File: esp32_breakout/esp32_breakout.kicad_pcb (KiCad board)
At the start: 2 copper layers, 73.1 x 33.1 mm, 29 parts, among them J1 JST B7B-PH-K-S, J2 JST B7B-PH-K-S, J3 JST B6B-PH-K-S, J4 XT30U-M, J5 JST B5B-PH-K-S, J6 DNP, J7 DNP, J8 JST B6B-ZR, J9 JST B6B-ZR, SW1 SS12D10, U1 ESP32 DEV KIT Module 30-pin, U2 LM2596 Module

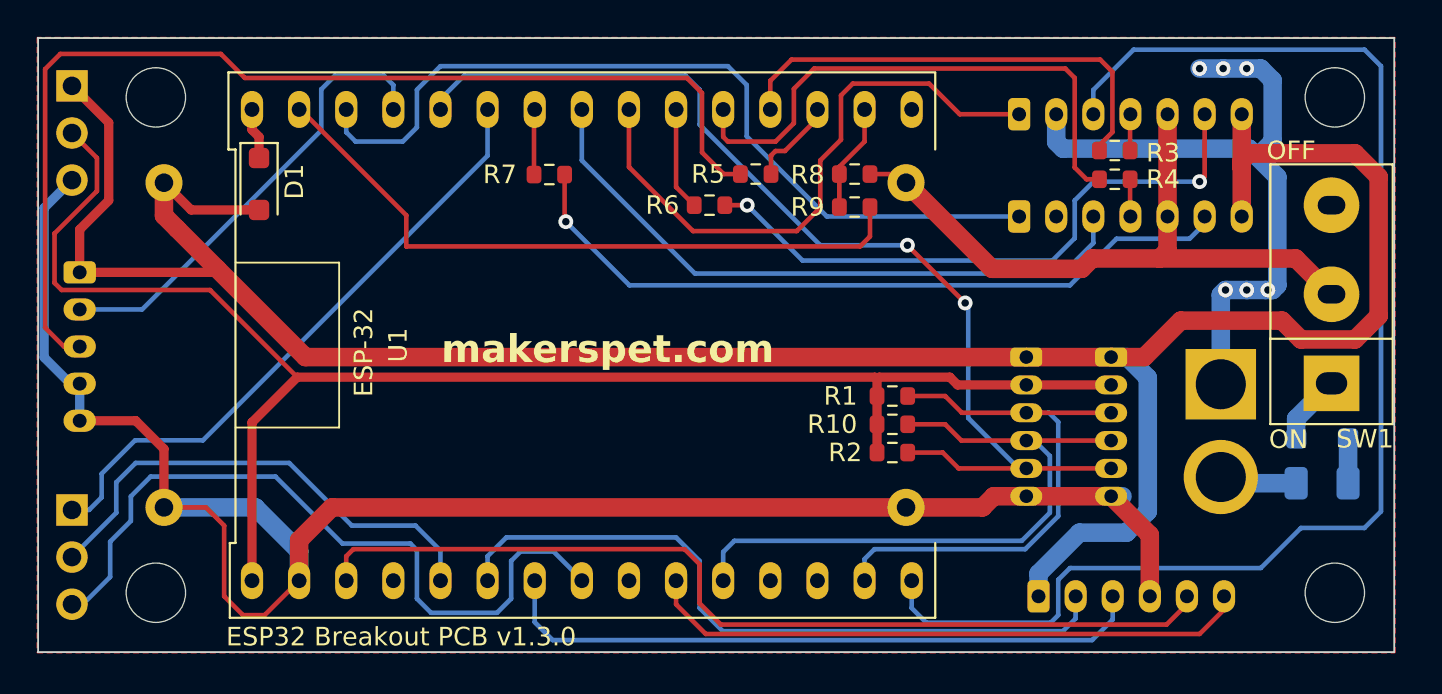
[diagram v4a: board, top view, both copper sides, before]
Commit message: ZH connectors
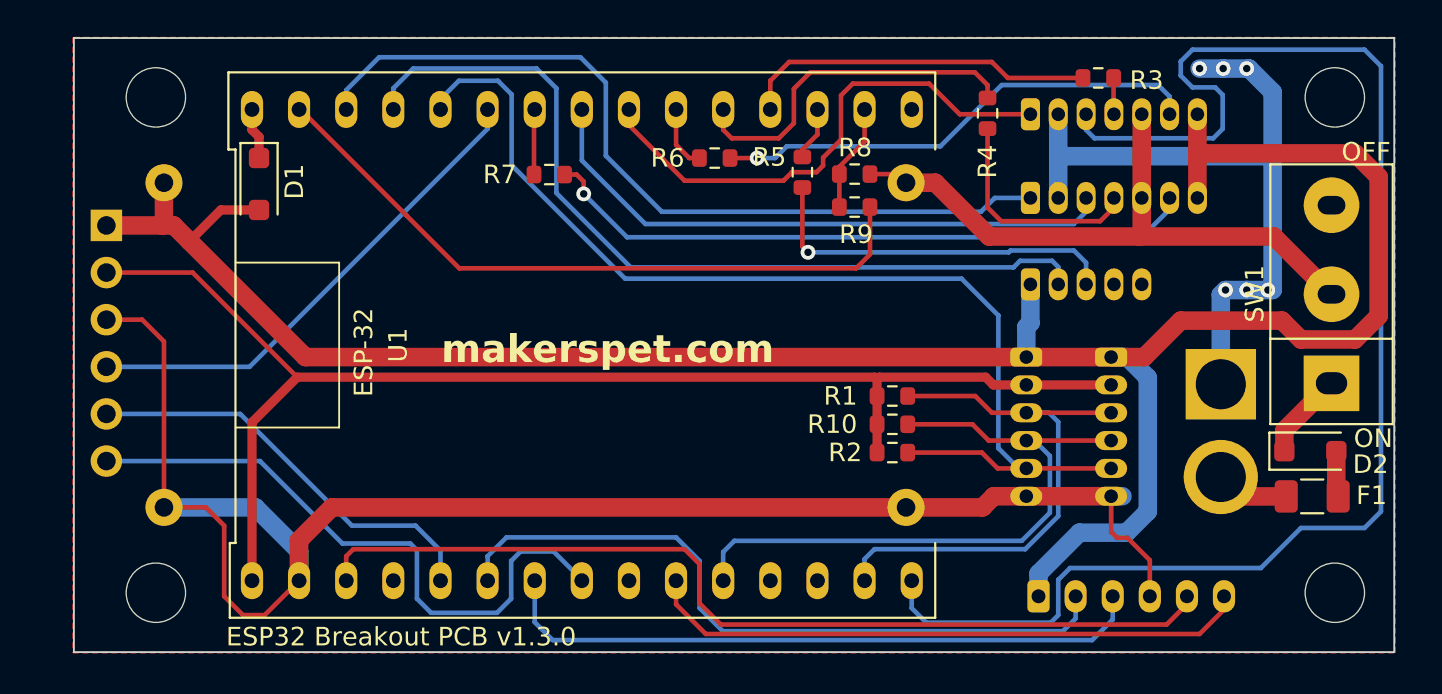
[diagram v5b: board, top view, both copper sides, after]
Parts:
- removed J7: DNP, Connector_PinSocket_2.54mm:PinSocket_1x03_P2.54mm_Vertical
- D2, F1: moved to F.Cu
- J1, J2: value JST B7B-PH-K-S -> JST B7B-ZR; footprint Connector_JST:JST_PH_B7B-PH-K_1x07_P2.00mm_Vertical -> Makerspet:JST_ZH_B7B-ZR_1x07_P1.50mm_Vertical
- J5: value JST B5B-PH-K-S -> JST B5B-ZR; footprint Connector_JST:JST_PH_B5B-PH-K_1x05_P2.00mm_Vertical -> Makerspet:JST_ZH_B5B-ZR_1x05_P1.50mm_Vertical
- J6: footprint Connector_PinSocket_2.54mm:PinSocket_1x03_P2.54mm_Vertical -> Connector_PinSocket_2.54mm:PinSocket_1x06_P2.54mm_Vertical
- moved J5 51.3 mm to (145.4, 61.9), turned to 0 degrees
- moved J6 15.4 mm to (95.6, 58.7)
- moved R4 7.73 mm to (143.1, 52.7), turned to -90 degrees
- moved R3 4.01 mm to (149.1, 50.8)
- moved R6 2.56 mm to (128.4, 55.1)
- moved R5 2.52 mm to (133.1, 55.9), turned to -90 degrees
- moved J1 1.17 mm to (145.4, 57.3)
- moved D2 0.93 mm to (160.5, 70.9)
- moved F1 0.89 mm to (160.6, 73.4)
- moved J2 0.61 mm to (145.4, 52.8)
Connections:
- J6 pad 1: /GPIO27 -> +5V
- J6 pad 2: /GPIO4 -> +3V3
- J6 pad 3: /GPIO5_BOOT_STRAP -> GND
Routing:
- net Net-(J5-Pin_3): track 58.6 -> 20.1 mm, vias 0 -> 1
- net /GPIO12_OUT_STRAP: track 24.9 -> 46.4 mm
- net +3V3: track 85.3 -> 73.1 mm
- net +5V: track 136.5 -> 124.6 mm
- net /MOT_FG_RIGHT_ENC_A: track 29.9 -> 19.1 mm
- net Net-(J1-Pin_4): track 2.01 -> 12.2 mm
- net GND: track 173.6 -> 166.2 mm
- net /MOT_CW_LEFT_IN2: track 72.8 -> 80.0 mm
- net Net-(J2-Pin_6): track 33.5 -> 26.5 mm, vias 2 -> 1
- net /GPIO27: track 33.6 -> 27.0 mm
- net /GPIO5_BOOT_STRAP: track 40.0 -> 33.7 mm
- net /MOT_FG_LEFT_ENC_A: track 25.2 -> 19.1 mm
- net Net-(J1-Pin_6): track 40.2 -> 35.6 mm
- net /MOT_PWM_LEFT_IN1: track 32.4 -> 28.2 mm
- net /GPIO4: track 26.5 -> 22.7 mm
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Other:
- board size 73.1 x 33.1 mm -> 71.2 x 33.1 mm
- board text added: "EXP"
- board text removed: "EXPANSION"
